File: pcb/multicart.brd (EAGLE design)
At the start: 58.1 x 87.6 mm, 14 parts, among them IC1 74HCT373N, IC2 M27C4001B, IC3 74HCT02N, IC4 74HCT00N

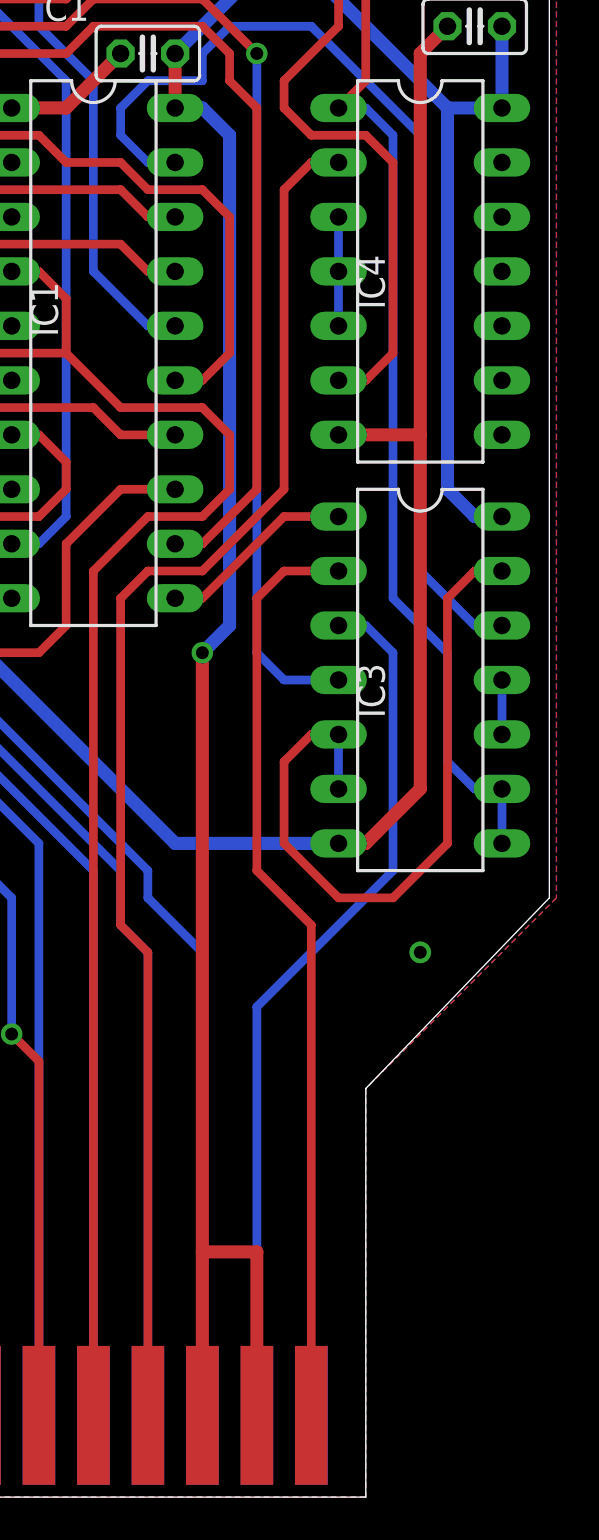
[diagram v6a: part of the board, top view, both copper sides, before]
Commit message: Added pull-downs to the CCTL & R/W lines.
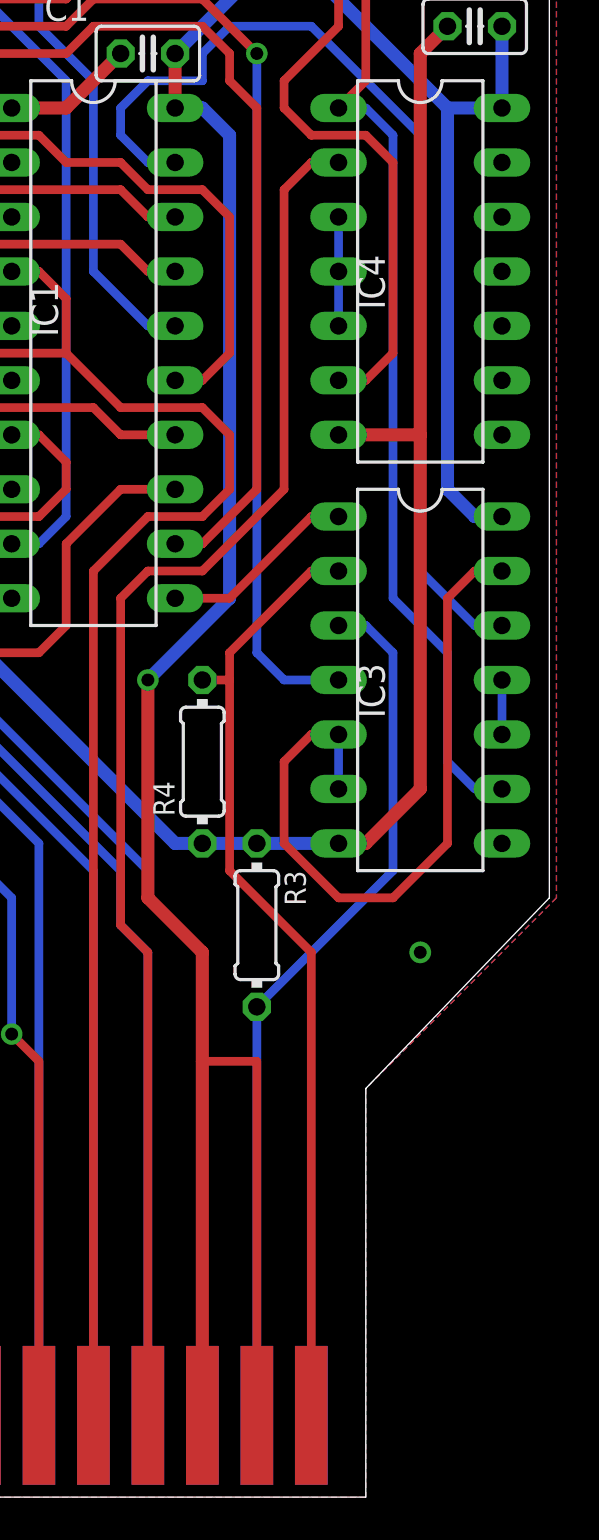
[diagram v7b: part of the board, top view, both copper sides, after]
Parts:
- added R3, R4: 4k7, resistor:0204/7
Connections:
- net GND: now also R3.1, R4.1
- net N$20: now also R3.2
- net N$8: now also R4.2
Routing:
- net VCC: track 164.7 -> 175.7 mm
- net N$19: track 186.4 -> 182.6 mm
- net N$8: track 43.5 -> 45.1 mm
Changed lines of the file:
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@@
 <layer number="42" name="bRestrict" color="1" fill="10" visible="no" active="yes"/>
 <layer number="43" name="vRestrict" color="2" fill="10" visible="no" active="yes"/>
-<layer number="44" name="Drills" color="7" fill="1" visible="yes" active="yes"/>
-<layer number="45" name="Holes" color="7" fill="1" visible="yes" active="yes"/>
-<layer number="46" name="Milling" color="3" fill="1" visible="yes" active="yes"/>
-<layer number="47" name="Measures" color="7" fill="1" visible="no" active="yes"/>
+<layer number="44" name="Drills" color="7" fill="1" visible="no" active="yes"/>
+<layer number="45" name="Holes" color="7" fill="1" visible="no" active="yes"/>
+<layer number="46" name="Milling" color="3" fill="1" visible="no" active="yes"/>
+<layer number="47" name="Measures" color="7" fill="1" visible="yes" active="yes"/>
 <layer number="48" name="Document" color="7" fill="1" visible="yes" active="yes"/>
 <layer number="49" name="Reference" color="7" fill="1" visible="yes" active="yes"/>
@@
 <attribute name="VALUE" x="61.976" y="68.834" size="1.27" layer="27" ratio="10" rot="R180"/>
 </element>
+<element name="R3" library="resistor" package="0204/7" value="4k7" x="49.53" y="24.13" rot="R270"/>
+<element name="R4" library="resistor" package="0204/7" value="4k7" x="46.99" y="31.75" rot="R90"/>
 </elements>
 <signals>
@@
 <contactref element="R2" pad="2"/>
 <contactref element="R5" pad="2"/>
-<wire x1="46.99" y1="36.83" x2="46.99" y2="8.89" width="0.6096" layer="1"/>
-<wire x1="46.99" y1="8.89" x2="46.99" y2="1.27" width="0.6096" layer="1"/>
 <wire x1="50.8" y1="69.85" x2="50.8" y2="72.39" width="0.6096" layer="16"/>
 <wire x1="48.26" y1="77.47" x2="48.26" y2="74.93" width="0.6096" layer="16"/>
@@
 <wire x1="45.72" y1="62.23" x2="45.72" y2="64.77" width="0.6096" layer="1"/>
 <contactref element="J1" pad="14"/>
-<wire x1="49.53" y1="1.27" x2="49.53" y2="8.89" width="0.6096" layer="1"/>
-<wire x1="49.53" y1="8.89" x2="46.99" y2="8.89" width="0.6096" layer="1"/>
-<via x="46.99" y="36.83" extent="1-16" drill="0.6" shape="octagon"/>
-<wire x1="46.99" y1="36.83" x2="48.26" y2="38.1" width="0.6096" layer="16"/>
-<wire x1="48.26" y1="38.1" x2="48.26" y2="60.96" width="0.6096" layer="16"/>
+<via x="44.45" y="35.56" extent="1-16" drill="0.6" shape="octagon"/>
 <wire x1="48.26" y1="60.96" x2="46.99" y2="62.23" width="0.6096" layer="16"/>
 <wire x1="46.99" y1="62.23" x2="45.72" y2="62.23" width="0.6096" layer="16"/>
+<wire x1="46.99" y1="1.27" x2="46.99" y2="17.78" width="0.6096" layer="1"/>
+<wire x1="46.99" y1="17.78" x2="46.99" y2="22.86" width="0.6096" layer="1"/>
+<wire x1="46.99" y1="22.86" x2="44.45" y2="25.4" width="0.6096" layer="1"/>
+<wire x1="44.45" y1="25.4" x2="44.45" y2="35.56" width="0.6096" layer="1"/>
+<wire x1="48.26" y1="39.37" x2="44.45" y2="35.56" width="0.6096" layer="16"/>
+<wire x1="48.26" y1="39.37" x2="48.26" y2="60.96" width="0.6096" layer="16"/>
+<wire x1="49.53" y1="1.27" x2="49.53" y2="17.78" width="0.4064" layer="1"/>
+<wire x1="49.53" y1="17.78" x2="46.99" y2="17.78" width="0.4064" layer="1"/>
 </signal>
 <signal name="GND">
@@
 <contactref element="C3" pad="2"/>
 <wire x1="25.4" y1="63.5" x2="31.75" y2="63.5" width="0.6096" layer="16"/>
-<wire x1="45.72" y1="27.94" x2="53.34" y2="27.94" width="0.6096" layer="16"/>
 <wire x1="54.61" y1="27.94" x2="53.34" y2="27.94" width="0.6096" layer="1"/>
 <wire x1="53.34" y1="46.99" x2="57.15" y2="46.99" width="0.6096" layer="1"/>
@@
 <via x="34.29" y="60.96" extent="1-16" drill="0.6" shape="octagon"/>
 <wire x1="34.29" y1="60.96" x2="31.75" y2="63.5" width="0.6096" layer="16"/>
-<wire x1="34.29" y1="39.37" x2="45.72" y2="27.94" width="0.6096" layer="16"/>
 <wire x1="38.1" y1="39.37" x2="34.29" y2="39.37" width="0.6096" layer="16"/>
 <wire x1="57.15" y1="64.77" x2="58.42" y2="66.04" width="0.6096" layer="1"/>
+<contactref element="R4" pad="1"/>
+<contactref element="R3" pad="1"/>
+<wire x1="53.34" y1="27.94" x2="49.53" y2="27.94" width="0.6096" layer="16"/>
+<wire x1="34.29" y1="39.37" x2="45.72" y2="27.94" width="0.6096" layer="16"/>
+<wire x1="45.72" y1="27.94" x2="46.99" y2="27.94" width="0.6096" layer="16"/>
+<wire x1="46.99" y1="27.94" x2="49.53" y2="27.94" width="0.6096" layer="16"/>
 </signal>
 <signal name="N$9">
@@
 <wire x1="44.45" y1="69.85" x2="48.26" y2="69.85" width="0.4064" layer="1"/>
 </signal>
-<signal name="N$7">
-<contactref element="IC1" pad="11"/>
-<contactref element="IC3" pad="1"/>
-<wire x1="45.72" y1="39.37" x2="46.99" y2="39.37" width="0.4064" layer="1"/>
-<wire x1="46.99" y1="39.37" x2="50.8" y2="43.18" width="0.4064" layer="1"/>
-<wire x1="50.8" y1="43.18" x2="53.34" y2="43.18" width="0.4064" layer="1"/>
-</signal>
 <signal name="N$8">
 <contactref element="J1" pad="15"/>
 <contactref element="IC3" pad="2"/>
-<wire x1="52.07" y1="1.27" x2="52.07" y2="24.13" width="0.4064" layer="1"/>
-<wire x1="52.07" y1="24.13" x2="49.53" y2="26.67" width="0.4064" layer="1"/>
-<wire x1="49.53" y1="26.67" x2="49.53" y2="39.37" width="0.4064" layer="1"/>
-<wire x1="49.53" y1="39.37" x2="50.8" y2="40.64" width="0.4064" layer="1"/>
-<wire x1="50.8" y1="40.64" x2="53.34" y2="40.64" width="0.4064" layer="1"/>
+<contactref element="R4" pad="2"/>
+<wire x1="52.07" y1="22.86" x2="52.07" y2="1.27" width="0.4064" layer="1"/>
+<wire x1="48.26" y1="36.83" x2="52.07" y2="40.64" width="0.4064" layer="1"/>
+<wire x1="52.07" y1="40.64" x2="53.34" y2="40.64" width="0.4064" layer="1"/>
+<wire x1="48.26" y1="35.56" x2="48.26" y2="36.83" width="0.4064" layer="1"/>
+<wire x1="46.99" y1="35.56" x2="48.26" y2="35.56" width="0.4064" layer="1"/>
+<wire x1="52.07" y1="22.86" x2="48.26" y2="26.67" width="0.4064" layer="1"/>
+<wire x1="48.26" y1="26.67" x2="48.26" y2="35.56" width="0.4064" layer="1"/>
 </signal>
 <signal name="N$21">
@@
 <contactref element="J1" pad="1"/>
 <contactref element="IC4" pad="1"/>
-<contactref element="IC3" pad="9"/>
 <contactref element="IC3" pad="8"/>
 <wire x1="55.88" y1="60.96" x2="55.88" y2="39.37" width="0.4064" layer="16"/>
@@
 <wire x1="58.42" y1="36.83" x2="58.42" y2="31.75" width="0.4064" layer="16"/>
 <wire x1="58.42" y1="31.75" x2="59.69" y2="30.48" width="0.4064" layer="16"/>
-<wire x1="59.69" y1="30.48" x2="60.96" y2="30.48" width="0.4064" layer="16"/>
-<wire x1="60.96" y1="30.48" x2="60.96" y2="27.94" width="0.4064" layer="16"/>
 <wire x1="6.35" y1="26.67" x2="6.35" y2="73.66" width="0.4064" layer="1"/>
 <wire x1="6.35" y1="73.66" x2="16.51" y2="83.82" width="0.4064" layer="1"/>
@@
 <wire x1="6.35" y1="26.67" x2="16.51" y2="16.51" width="0.4064" layer="1"/>
 <wire x1="16.51" y1="16.51" x2="16.51" y2="1.27" width="0.4064" layer="1"/>
+<contactref element="IC3" pad="9"/>
+<wire x1="59.69" y1="30.48" x2="60.96" y2="30.48" width="0" layer="19" extent="16-16"/>
+<wire x1="60.96" y1="27.94" x2="60.96" y2="30.48" width="0" layer="19" extent="1-1"/>
 </signal>
 <signal name="N$20">
 <contactref element="J1" pad="R"/>
 <contactref element="IC3" pad="3"/>
-<wire x1="49.53" y1="1.27" x2="49.53" y2="20.32" width="0.4064" layer="16"/>
 <wire x1="53.34" y1="38.1" x2="54.61" y2="38.1" width="0.4064" layer="16"/>
 <wire x1="54.61" y1="38.1" x2="55.88" y2="36.83" width="0.4064" layer="16"/>
 <wire x1="55.88" y1="36.83" x2="55.88" y2="26.67" width="0.4064" layer="16"/>
-<wire x1="55.88" y1="26.67" x2="49.53" y2="20.32" width="0.4064" layer="16"/>
+<contactref element="R3" pad="2"/>
+<wire x1="49.53" y1="1.27" x2="49.53" y2="20.32" width="0.4064" layer="16"/>
+<wire x1="49.53" y1="20.32" x2="55.88" y2="26.67" width="0.4064" layer="16"/>
 </signal>
 <signal name="N$17">
@@
 <wire x1="50.8" y1="62.23" x2="50.8" y2="63.5" width="0.4064" layer="1"/>
 </signal>
+<signal name="N$7">
+<contactref element="IC3" pad="1"/>
+<contactref element="IC1" pad="11"/>
+<wire x1="45.72" y1="39.37" x2="48.26" y2="39.37" width="0.4064" layer="1"/>
+<wire x1="48.26" y1="39.37" x2="52.07" y2="43.18" width="0.4064" layer="1"/>
+<wire x1="52.07" y1="43.18" x2="53.34" y2="43.18" width="0.4064" layer="1"/>
+</signal>
 </signals>

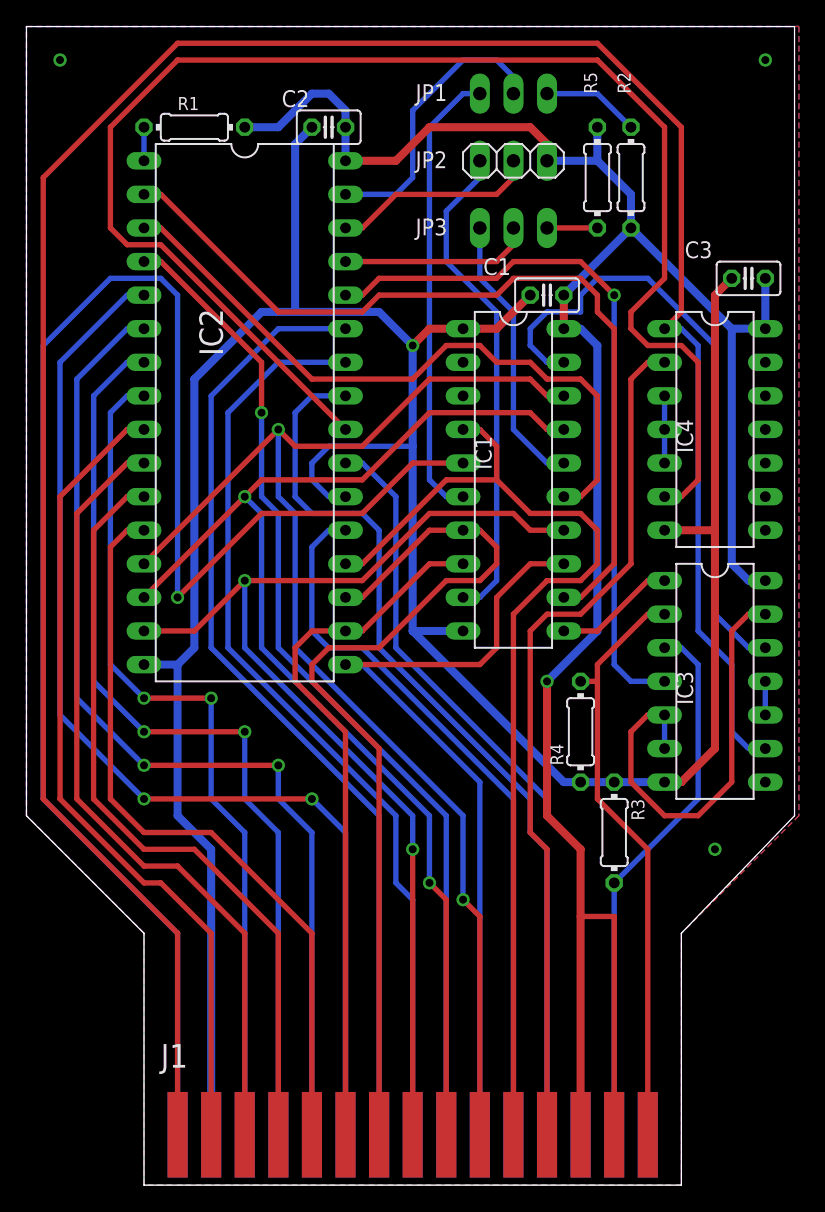
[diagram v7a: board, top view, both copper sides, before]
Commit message: Optimized the design by using AND gates.
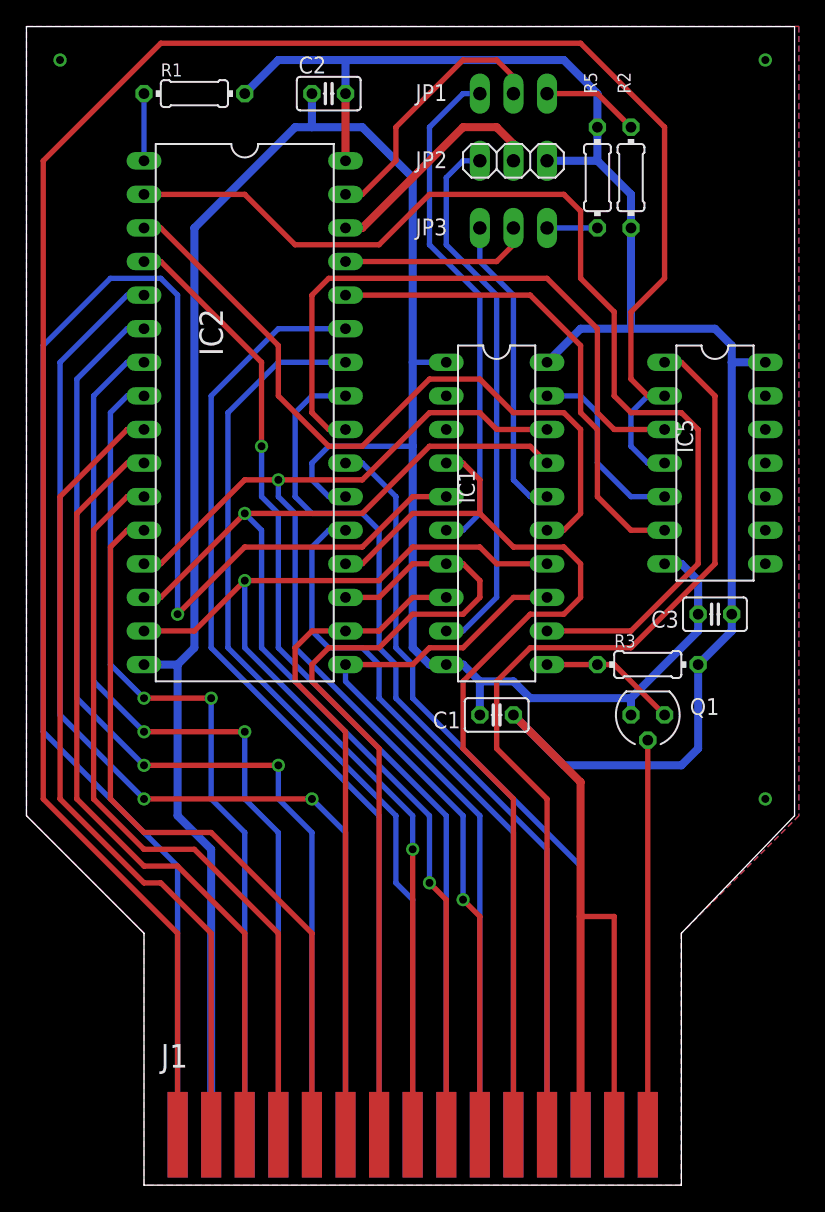
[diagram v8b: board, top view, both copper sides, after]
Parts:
- removed IC3: 74HCT02N, 74xx-eu:DIL14
- removed IC4: 74HCT00N, 74xx-eu:DIL14
- removed R4: 4k7, resistor:0204/7
- added IC5: 74HCT08N, 74xx-eu:DIL14
- added Q1: BS170, transistor-small-signal:SOT54E
- moved C1 32.0 mm to (40.6, 33.0)
- moved C3 25.5 mm to (57.1, 40.6)
- moved R3 13.0 mm to (52.1, 36.8), turned to 180 degrees
- moved IC1 2.84 mm to (40.6, 48.3)
- moved C2 2.54 mm to (27.9, 80.0)
- moved R1 2.54 mm to (17.8, 80.0)
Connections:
- removed net N$14: IC4.3, IC4.4, IC4.5
- removed net N$17: IC3.10, IC3.11
- removed net N$20: IC3.3, J1.R, R3.2
- removed net N$23: IC3.13, IC3.5, IC3.6
- net GND: now also IC5.7, Q1.S; no longer IC3.7, IC4.7, R3.1, R4.1
- net N$1: now also IC5.5; no longer IC3.12
- net N$18: now also IC5.1; no longer IC4.2
- net N$19: now also IC5.2, IC5.4; no longer IC3.8, IC3.9, IC4.1
- net N$21: now also IC5.6; no longer IC3.4
- net N$27: now also IC5.3; no longer IC4.6
- net N$7: now also Q1.D, R3.2; no longer IC3.1
- net N$8: now also Q1.G; no longer IC3.2, R4.2
- net VCC: now also IC5.14, R3.1; no longer IC3.14, IC4.14
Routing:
- net N$27: track 112.2 -> 47.6 mm
- net N$20: track 41.3 -> 0.00 mm
- net N$23: track 33.6 -> 0.00 mm
- net N$1: track 47.9 -> 14.3 mm
- net GND: track 213.6 -> 184.3 mm, vias 1 -> 0
- net N$19: track 182.6 -> 163.0 mm
- net N$4: track 65.3 -> 82.8 mm
- net N$21: track 54.7 -> 37.4 mm, vias 1 -> 0
- net N$8: track 45.1 -> 29.8 mm
- net N$18: track 65.4 -> 73.6 mm
- net D0: track 98.8 -> 91.6 mm
- net D3: track 62.4 -> 57.1 mm
- net N$14: track 5.08 -> 0.00 mm
- net D5: track 70.1 -> 65.5 mm
- net N$3: track 51.1 -> 55.2 mm
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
